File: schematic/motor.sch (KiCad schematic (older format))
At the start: 23 parts, among them U2 TMC2130

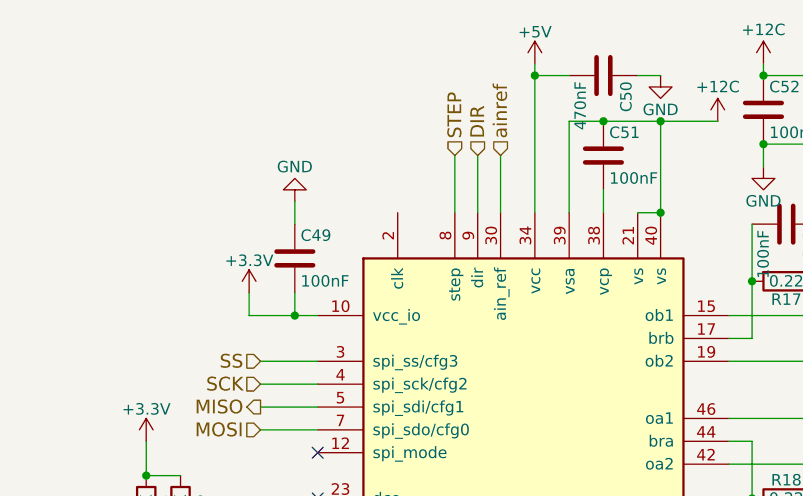
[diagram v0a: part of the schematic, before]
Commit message: Removed some components
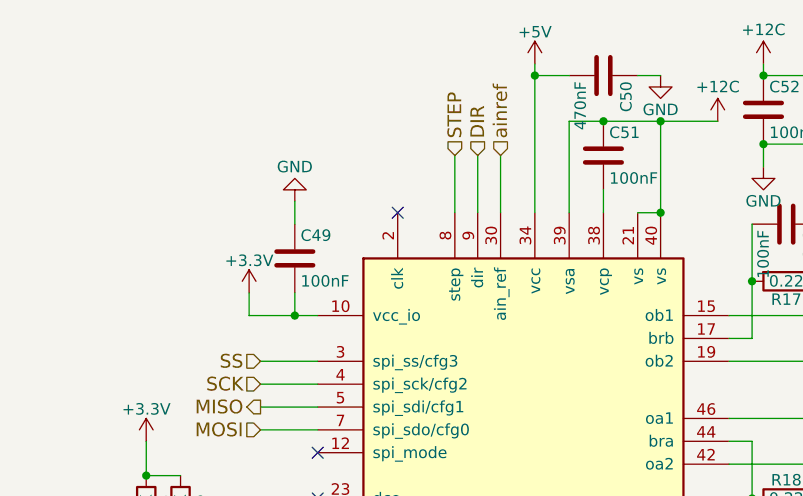
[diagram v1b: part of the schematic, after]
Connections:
- no-connect marks 3 -> 4
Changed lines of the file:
@@
 $Descr A4 11693 8268
 encoding utf-8
-Sheet 1 10
+Sheet 4 10
 Title ""
 Date ""
@@
 DIAG1
 $Comp
-L GND #PWR14
+L GND #PWR27
 U 1 1 59E7A6C8
 P 4050 3700
-AR Path="/59E79F4A/59E7A6C8" Ref="#PWR14"  Part="1"
-AR Path="/59E85192/59E7A6C8" Ref="#PWR29"  Part="1"
-AR Path="/59E85CD9/59E7A6C8" Ref="#PWR44"  Part="1"
-AR Path="/59E88785/59E7A6C8" Ref="#PWR59"  Part="1"
-F 0 "#PWR59" H 4050 3450 50  0001 C CNN
+AR Path="/59E79F4A/59E7A6C8" Ref="#PWR27"  Part="1"
+AR Path="/59E85192/59E7A6C8" Ref="#PWR42"  Part="1"
+AR Path="/59E85CD9/59E7A6C8" Ref="#PWR57"  Part="1"
+AR Path="/59E88785/59E7A6C8" Ref="#PWR72"  Part="1"
+F 0 "#PWR72" H 4050 3450 50  0001 C CNN
 F 1 "GND" H 4050 3550 50  0000 C CNN
 F 2 "" H 4050 3700 50  0001 C CNN
@@
 $EndComp
 $Comp
-L +3.3V #PWR12
+L +3.3V #PWR25
 U 1 1 59E7ABA2
 P 3550 3350
-AR Path="/59E79F4A/59E7ABA2" Ref="#PWR12"  Part="1"
-AR Path="/59E85192/59E7ABA2" Ref="#PWR27"  Part="1"
-AR Path="/59E85CD9/59E7ABA2" Ref="#PWR42"  Part="1"
-AR Path="/59E88785/59E7ABA2" Ref="#PWR57"  Part="1"
-F 0 "#PWR57" H 3550 3200 50  0001 C CNN
+AR Path="/59E79F4A/59E7ABA2" Ref="#PWR25"  Part="1"
+AR Path="/59E85192/59E7ABA2" Ref="#PWR40"  Part="1"
+AR Path="/59E85CD9/59E7ABA2" Ref="#PWR55"  Part="1"
+AR Path="/59E88785/59E7ABA2" Ref="#PWR70"  Part="1"
+F 0 "#PWR70" H 3550 3200 50  0001 C CNN
 F 1 "+3.3V" H 3550 3490 50  0000 C CNN
 F 2 "" H 3550 3350 50  0001 C CNN
@@
 DIR
 $Comp
-L GND #PWR16
+L GND #PWR29
 U 1 1 59E7AD62
 P 4200 4800
-AR Path="/59E79F4A/59E7AD62" Ref="#PWR16"  Part="1"
-AR Path="/59E85192/59E7AD62" Ref="#PWR31"  Part="1"
-AR Path="/59E85CD9/59E7AD62" Ref="#PWR46"  Part="1"
-AR Path="/59E88785/59E7AD62" Ref="#PWR61"  Part="1"
-F 0 "#PWR61" H 4200 4550 50  0001 C CNN
+AR Path="/59E79F4A/59E7AD62" Ref="#PWR29"  Part="1"
+AR Path="/59E85192/59E7AD62" Ref="#PWR44"  Part="1"
+AR Path="/59E85CD9/59E7AD62" Ref="#PWR59"  Part="1"
+AR Path="/59E88785/59E7AD62" Ref="#PWR74"  Part="1"
+F 0 "#PWR74" H 4200 4550 50  0001 C CNN
 F 1 "GND" H 4200 4650 50  0000 C CNN
 F 2 "" H 4200 4800 50  0001 C CNN
@@
 $EndComp
 $Comp
-L GND #PWR17
+L GND #PWR30
 U 1 1 59E7AE9D
 P 4600 5300
-AR Path="/59E79F4A/59E7AE9D" Ref="#PWR17"  Part="1"
-AR Path="/59E85192/59E7AE9D" Ref="#PWR32"  Part="1"
-AR Path="/59E85CD9/59E7AE9D" Ref="#PWR47"  Part="1"
-AR Path="/59E88785/59E7AE9D" Ref="#PWR62"  Part="1"
-F 0 "#PWR62" H 4600 5050 50  0001 C CNN
+AR Path="/59E79F4A/59E7AE9D" Ref="#PWR30"  Part="1"
+AR Path="/59E85192/59E7AE9D" Ref="#PWR45"  Part="1"
+AR Path="/59E85CD9/59E7AE9D" Ref="#PWR60"  Part="1"
+AR Path="/59E88785/59E7AE9D" Ref="#PWR75"  Part="1"
+F 0 "#PWR75" H 4600 5050 50  0001 C CNN
 F 1 "GND" H 4600 5150 50  0000 C CNN
 F 2 "" H 4600 5300 50  0001 C CNN
@@
 $EndComp
 $Comp
-L +5V #PWR18
+L +5V #PWR16
 U 1 1 59E7B341
 P 5250 1700
-AR Path="/59E79F4A/59E7B341" Ref="#PWR18"  Part="1"
-AR Path="/59E85192/59E7B341" Ref="#PWR33"  Part="1"
-AR Path="/59E85CD9/59E7B341" Ref="#PWR48"  Part="1"
-AR Path="/59E88785/59E7B341" Ref="#PWR63"  Part="1"
-F 0 "#PWR63" H 5250 1550 50  0001 C CNN
+AR Path="/59E79F4A/59E7B341" Ref="#PWR16"  Part="1"
+AR Path="/59E85192/59E7B341" Ref="#PWR31"  Part="1"
+AR Path="/59E85CD9/59E7B341" Ref="#PWR46"  Part="1"
+AR Path="/59E88785/59E7B341" Ref="#PWR61"  Part="1"
+F 0 "#PWR61" H 5250 1550 50  0001 C CNN
 F 1 "+5V" H 5250 1840 50  0000 C CNN
 F 2 "" H 5250 1700 50  0001 C CNN
@@
 $EndComp
 $Comp
-L +3.3V #PWR13
+L +3.3V #PWR23
 U 1 1 59E7B49B
 P 4000 2700
-AR Path="/59E79F4A/59E7B49B" Ref="#PWR13"  Part="1"
-AR Path="/59E85192/59E7B49B" Ref="#PWR28"  Part="1"
-AR Path="/59E85CD9/59E7B49B" Ref="#PWR43"  Part="1"
-AR Path="/59E88785/59E7B49B" Ref="#PWR58"  Part="1"
-F 0 "#PWR58" H 4000 2550 50  0001 C CNN
+AR Path="/59E79F4A/59E7B49B" Ref="#PWR23"  Part="1"
+AR Path="/59E85192/59E7B49B" Ref="#PWR38"  Part="1"
+AR Path="/59E85CD9/59E7B49B" Ref="#PWR53"  Part="1"
+AR Path="/59E88785/59E7B49B" Ref="#PWR68"  Part="1"
+F 0 "#PWR68" H 4000 2550 50  0001 C CNN
 F 1 "+3.3V" H 4000 2840 50  0000 C CNN
 F 2 "" H 4000 2700 50  0001 C CNN
@@
 $EndComp
 $Comp
-L GND #PWR15
+L GND #PWR21
 U 1 1 59E7B4C1
 P 4200 2300
-AR Path="/59E79F4A/59E7B4C1" Ref="#PWR15"  Part="1"
-AR Path="/59E85192/59E7B4C1" Ref="#PWR30"  Part="1"
-AR Path="/59E85CD9/59E7B4C1" Ref="#PWR45"  Part="1"
-AR Path="/59E88785/59E7B4C1" Ref="#PWR60"  Part="1"
-F 0 "#PWR60" H 4200 2050 50  0001 C CNN
+AR Path="/59E79F4A/59E7B4C1" Ref="#PWR21"  Part="1"
+AR Path="/59E85192/59E7B4C1" Ref="#PWR36"  Part="1"
+AR Path="/59E85CD9/59E7B4C1" Ref="#PWR51"  Part="1"
+AR Path="/59E88785/59E7B4C1" Ref="#PWR66"  Part="1"
+F 0 "#PWR66" H 4200 2050 50  0001 C CNN
 F 1 "GND" H 4200 2150 50  0000 C CNN
 F 2 "" H 4200 2300 50  0001 C CNN
@@
 $EndComp
 $Comp
-L GND #PWR19
+L GND #PWR18
 U 1 1 59E7B858
 P 5800 1750
-AR Path="/59E79F4A/59E7B858" Ref="#PWR19"  Part="1"
-AR Path="/59E85192/59E7B858" Ref="#PWR34"  Part="1"
-AR Path="/59E85CD9/59E7B858" Ref="#PWR49"  Part="1"
-AR Path="/59E88785/59E7B858" Ref="#PWR64"  Part="1"
-F 0 "#PWR64" H 5800 1500 50  0001 C CNN
+AR Path="/59E79F4A/59E7B858" Ref="#PWR18"  Part="1"
+AR Path="/59E85192/59E7B858" Ref="#PWR33"  Part="1"
+AR Path="/59E85CD9/59E7B858" Ref="#PWR48"  Part="1"
+AR Path="/59E88785/59E7B858" Ref="#PWR63"  Part="1"
+F 0 "#PWR63" H 5800 1500 50  0001 C CNN
 F 1 "GND" H 5800 1600 50  0000 C CNN
 F 2 "" H 5800 1750 50  0001 C CNN
@@
 $EndComp
 $Comp
-L GND #PWR25
+L GND #PWR24
 U 1 1 59E7C836
 P 7850 2900
-AR Path="/59E79F4A/59E7C836" Ref="#PWR25"  Part="1"
-AR Path="/59E85192/59E7C836" Ref="#PWR40"  Part="1"
-AR Path="/59E85CD9/59E7C836" Ref="#PWR55"  Part="1"
-AR Path="/59E88785/59E7C836" Ref="#PWR70"  Part="1"
-F 0 "#PWR70" H 7850 2650 50  0001 C CNN
+AR Path="/59E79F4A/59E7C836" Ref="#PWR24"  Part="1"
+AR Path="/59E85192/59E7C836" Ref="#PWR39"  Part="1"
+AR Path="/59E85CD9/59E7C836" Ref="#PWR54"  Part="1"
+AR Path="/59E88785/59E7C836" Ref="#PWR69"  Part="1"
+F 0 "#PWR69" H 7850 2650 50  0001 C CNN
 F 1 "GND" H 7850 2750 50  0000 C CNN
 F 2 "" H 7850 2900 50  0001 C CNN
@@
 $EndComp
 $Comp
-L GND #PWR23
+L GND #PWR22
 U 1 1 59E7CE35
 P 6650 2550
-AR Path="/59E79F4A/59E7CE35" Ref="#PWR23"  Part="1"
-AR Path="/59E85192/59E7CE35" Ref="#PWR38"  Part="1"
-AR Path="/59E85CD9/59E7CE35" Ref="#PWR53"  Part="1"
-AR Path="/59E88785/59E7CE35" Ref="#PWR68"  Part="1"
-F 0 "#PWR68" H 6650 2300 50  0001 C CNN
+AR Path="/59E79F4A/59E7CE35" Ref="#PWR22"  Part="1"
+AR Path="/59E85192/59E7CE35" Ref="#PWR37"  Part="1"
+AR Path="/59E85CD9/59E7CE35" Ref="#PWR52"  Part="1"
+AR Path="/59E88785/59E7CE35" Ref="#PWR67"  Part="1"
+F 0 "#PWR67" H 6650 2300 50  0001 C CNN
 F 1 "GND" H 6650 2400 50  0000 C CNN
 F 2 "" H 6650 2550 50  0001 C CNN
@@
 $EndComp
 $Comp
-L GND #PWR24
+L GND #PWR28
 U 1 1 59E7D5D6
 P 6650 3700
-AR Path="/59E79F4A/59E7D5D6" Ref="#PWR24"  Part="1"
-AR Path="/59E85192/59E7D5D6" Ref="#PWR39"  Part="1"
-AR Path="/59E85CD9/59E7D5D6" Ref="#PWR54"  Part="1"
-AR Path="/59E88785/59E7D5D6" Ref="#PWR69"  Part="1"
-F 0 "#PWR69" H 6650 3450 50  0001 C CNN
+AR Path="/59E79F4A/59E7D5D6" Ref="#PWR28"  Part="1"
+AR Path="/59E85192/59E7D5D6" Ref="#PWR43"  Part="1"
+AR Path="/59E85CD9/59E7D5D6" Ref="#PWR58"  Part="1"
+AR Path="/59E88785/59E7D5D6" Ref="#PWR73"  Part="1"
+F 0 "#PWR73" H 6650 3450 50  0001 C CNN
 F 1 "GND" H 6650 3550 50  0000 C CNN
 F 2 "" H 6650 3700 50  0001 C CNN
@@
 Connection ~ 4950 5150
 $Comp
-L +12C #PWR66
+L +12C #PWR62
 U 1 1 5A02A4C9
 P 6250 1700
-AR Path="/59E88785/5A02A4C9" Ref="#PWR66"  Part="1"
-AR Path="/59E79F4A/5A02A4C9" Ref="#PWR21"  Part="1"
-AR Path="/59E85192/5A02A4C9" Ref="#PWR36"  Part="1"
-AR Path="/59E85CD9/5A02A4C9" Ref="#PWR51"  Part="1"
-F 0 "#PWR66" H 6250 1550 50  0001 C CNN
+AR Path="/59E88785/5A02A4C9" Ref="#PWR62"  Part="1"
+AR Path="/59E79F4A/5A02A4C9" Ref="#PWR17"  Part="1"
+AR Path="/59E85192/5A02A4C9" Ref="#PWR32"  Part="1"
+AR Path="/59E85CD9/5A02A4C9" Ref="#PWR47"  Part="1"
+F 0 "#PWR62" H 6250 1550 50  0001 C CNN
 F 1 "+12C" H 6250 1850 50  0000 C CNN
 F 2 "" H 6250 1700 50  0001 C CNN
@@
 $EndComp
 $Comp
-L +12C #PWR65
+L +12C #PWR64
 U 1 1 5A02A509
 P 6050 1950
-AR Path="/59E88785/5A02A509" Ref="#PWR65"  Part="1"
-AR Path="/59E79F4A/5A02A509" Ref="#PWR20"  Part="1"
-AR Path="/59E85192/5A02A509" Ref="#PWR35"  Part="1"
-AR Path="/59E85CD9/5A02A509" Ref="#PWR50"  Part="1"
-F 0 "#PWR65" H 6050 1800 50  0001 C CNN
+AR Path="/59E88785/5A02A509" Ref="#PWR64"  Part="1"
+AR Path="/59E79F4A/5A02A509" Ref="#PWR19"  Part="1"
+AR Path="/59E85192/5A02A509" Ref="#PWR34"  Part="1"
+AR Path="/59E85CD9/5A02A509" Ref="#PWR49"  Part="1"
+F 0 "#PWR64" H 6050 1800 50  0001 C CNN
 F 1 "+12C" H 6050 2100 50  0000 C CNN
 F 2 "" H 6050 1950 50  0001 C CNN
@@
 $EndComp
 $Comp
-L GND #PWR22
+L GND #PWR20
 U 1 1 5A02AD70
 P 6250 2150
-AR Path="/59E79F4A/5A02AD70" Ref="#PWR22"  Part="1"
-AR Path="/59E85192/5A02AD70" Ref="#PWR37"  Part="1"
-AR Path="/59E85CD9/5A02AD70" Ref="#PWR52"  Part="1"
-AR Path="/59E88785/5A02AD70" Ref="#PWR67"  Part="1"
-F 0 "#PWR67" H 6250 1900 50  0001 C CNN
+AR Path="/59E79F4A/5A02AD70" Ref="#PWR20"  Part="1"
+AR Path="/59E85192/5A02AD70" Ref="#PWR35"  Part="1"
+AR Path="/59E85CD9/5A02AD70" Ref="#PWR50"  Part="1"
+AR Path="/59E88785/5A02AD70" Ref="#PWR65"  Part="1"
+F 0 "#PWR65" H 6250 1900 50  0001 C CNN
 F 1 "GND" H 6250 2000 50  0000 C CNN
 F 2 "" H 6250 2150 50  0001 C CNN
@@
 	1    0    0    -1
 $EndComp
+NoConn ~ 4650 2350
 $EndSCHEMATC

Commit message: Updated to kicad v5
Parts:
- C10, C11, C12, C13, C14, C16, C17, C18, C19, C6, C7, C8, C9: symbol C -> schematic-rescue:C
- C15: symbol CP -> schematic-rescue:CP
- L1, L2, L3, L4: symbol Ferrite_Bead_Small -> schematic-rescue:Ferrite_Bead_Small
- R3, R4, R5, R6: symbol R -> schematic-rescue:R
- U2: symbol TMC2130 -> tmc2130:TMC2130
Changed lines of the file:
@@
-EESchema Schematic File Version 2
-LIBS:bd9e302efj
-LIBS:psmn1
-LIBS:tmc2130
-LIBS:74xgxx
-LIBS:74xx
-LIBS:ac-dc
-LIBS:actel
-LIBS:adc-dac
-LIBS:allegro
-LIBS:Altera
-LIBS:analog_devices
-LIBS:analog_switches
-LIBS:atmel
-LIBS:audio
-LIBS:battery_management
-LIBS:bbd
-LIBS:bosch
-LIBS:brooktre
-LIBS:cmos4000
-LIBS:cmos_ieee
-LIBS:conn
-LIBS:contrib
-LIBS:cypress
-LIBS:dc-dc
-LIBS:device
-LIBS:digital-audio
-LIBS:diode
-LIBS:display
-LIBS:dsp
-LIBS:elec-unifil
-LIBS:ESD_Protection
-LIBS:ftdi
-LIBS:gennum
-LIBS:graphic_symbols
-LIBS:hc11
-LIBS:infineon
-LIBS:intel
-LIBS:interface
-LIBS:intersil
-LIBS:ir
-LIBS:Lattice
-LIBS:leds
-LIBS:LEM
-LIBS:linear
-LIBS:logic_programmable
-LIBS:maxim
-LIBS:mechanical
-LIBS:memory
-LIBS:microchip
-LIBS:microchip_dspic33dsc
-LIBS:microchip_pic10mcu
-LIBS:microchip_pic12mcu
-LIBS:microchip_pic16mcu
-LIBS:microchip_pic18mcu
-LIBS:microchip_pic24mcu
-LIBS:microchip_pic32mcu
-LIBS:microcontrollers
-LIBS:modules
-LIBS:motor_drivers
-LIBS:motorola
-LIBS:motors
-LIBS:msp430
-LIBS:nordicsemi
-LIBS:nxp
-LIBS:nxp_armmcu
-LIBS:onsemi
-LIBS:opto
-LIBS:Oscillators
-LIBS:philips
-LIBS:power
-LIBS:powerint
-LIBS:Power_Management
-LIBS:pspice
-LIBS:references
-LIBS:regul
-LIBS:relays
-LIBS:rfcom
-LIBS:RFSolutions
-LIBS:sensors
-LIBS:silabs
-LIBS:siliconi
-LIBS:stm8
-LIBS:stm32
-LIBS:supertex
-LIBS:switches
-LIBS:texas
-LIBS:transf
-LIBS:transistors
-LIBS:triac_thyristor
-LIBS:ttl_ieee
-LIBS:valves
-LIBS:video
-LIBS:wiznet
-LIBS:Worldsemi
-LIBS:Xicor
-LIBS:xilinx
-LIBS:zetex
-LIBS:Zilog
+EESchema Schematic File Version 4
 LIBS:schematic-cache
-EELAYER 25 0
+EELAYER 26 0
 EELAYER END
 $Descr A4 11693 8268
@@
 SCK
 $Comp
-L TMC2130 U2
+L tmc2130:TMC2130 U2
 U 1 1 59E7A3F7
 P 5200 3750
@@
 DIAG1
 $Comp
-L GND #PWR017
+L power:GND #PWR017
 U 1 1 59E7A6C8
 P 4050 3700
@@
 DIAG0
 $Comp
-L R R4
+L schematic-rescue:R R4
 U 1 1 59E7AAF8
 P 3700 3650
@@
 $EndComp
 $Comp
-L R R3
+L schematic-rescue:R R3
 U 1 1 59E7AB4D
 P 3550 3650
@@
 $EndComp
 $Comp
-L +3.3V #PWR018
+L power:+3.3V #PWR018
 U 1 1 59E7ABA2
 P 3550 3350
@@
 DIR
 $Comp
-L GND #PWR019
+L power:GND #PWR019
 U 1 1 59E7AD62
 P 4200 4800
@@
 $EndComp
 $Comp
-L GND #PWR020
+L power:GND #PWR020
 U 1 1 59E7AE9D
 P 4600 5300
@@
 $EndComp
 $Comp
-L C C9
+L schematic-rescue:C C9
 U 1 1 59E7B152
 P 5550 2100
@@
 AR Path="/59E85CD9/59E7B152" Ref="C37"  Part="1"
 AR Path="/59E88785/59E7B152" Ref="C51"  Part="1"
+AR Path="/59E7B152" Ref="C51"  Part="1"
 F 0 "C51" H 5575 2200 50  0000 L CNN
 F 1 "100nF" H 5575 2000 50  0000 L CNN
@@
 $EndComp
 $Comp
-L +5V #PWR021
+L power:+5V #PWR021
 U 1 1 59E7B341
 P 5250 1700
@@
 $EndComp
 $Comp
-L C C7
+L schematic-rescue:C C7
 U 1 1 59E7B40E
 P 4200 2550
@@
 AR Path="/59E85CD9/59E7B40E" Ref="C35"  Part="1"
 AR Path="/59E88785/59E7B40E" Ref="C49"  Part="1"
+AR Path="/59E7B40E" Ref="C49"  Part="1"
 F 0 "C49" H 4225 2650 50  0000 L CNN
 F 1 "100nF" H 4225 2450 50  0000 L CNN
@@
 $EndComp
 $Comp
-L +3.3V #PWR022
+L power:+3.3V #PWR022
 U 1 1 59E7B49B
 P 4000 2700
@@
 $EndComp
 $Comp
-L GND #PWR023
+L power:GND #PWR023
 U 1 1 59E7B4C1
 P 4200 2300
@@
 $EndComp
 $Comp
-L C C6
+L schematic-rescue:C C6
 U 1 1 59E7B5DB
 P 3900 4500
@@
 AR Path="/59E85CD9/59E7B5DB" Ref="C34"  Part="1"
 AR Path="/59E88785/59E7B5DB" Ref="C48"  Part="1"
+AR Path="/59E7B5DB" Ref="C48"  Part="1"
 F 0 "C48" H 3925 4600 50  0000 L CNN
 F 1 "4.7uF" H 3925 4400 50  0000 L CNN
@@
 $EndComp
 $Comp
-L C C8
+L schematic-rescue:C C8
 U 1 1 59E7B7C5
 P 5550 1750
@@
 AR Path="/59E85CD9/59E7B7C5" Ref="C36"  Part="1"
 AR Path="/59E88785/59E7B7C5" Ref="C50"  Part="1"
+AR Path="/59E7B7C5" Ref="C50"  Part="1"
 F 0 "C50" H 5575 1850 50  0000 L CNN
 F 1 "470nF" H 5575 1650 50  0000 L CNN
@@
 $EndComp
 $Comp
-L GND #PWR024
+L power:GND #PWR024
 U 1 1 59E7B858
 P 5800 1750
@@
 $EndComp
 $Comp
-L C C10
+L schematic-rescue:C C10
 U 1 1 59E7BC4E
 P 6250 1900
@@
 AR Path="/59E85CD9/59E7BC4E" Ref="C38"  Part="1"
 AR Path="/59E88785/59E7BC4E" Ref="C52"  Part="1"
+AR Path="/59E7BC4E" Ref="C52"  Part="1"
 F 0 "C52" H 6275 2000 50  0000 L CNN
 F 1 "100nF" H 6275 1800 50  0000 L CNN
@@
 $EndComp
 $Comp
-L C C14
+L schematic-rescue:C C14
 U 1 1 59E7BC86
 P 6550 1900
@@
 AR Path="/59E85CD9/59E7BC86" Ref="C42"  Part="1"
 AR Path="/59E88785/59E7BC86" Ref="C56"  Part="1"
+AR Path="/59E7BC86" Ref="C56"  Part="1"
 F 0 "C56" H 6575 2000 50  0000 L CNN
 F 1 "100nF" H 6575 1800 50  0000 L CNN
@@
 $EndComp
 $Comp
-L CP C15
+L schematic-rescue:CP C15
 U 1 1 59E7BCBF
 P 6850 1900
@@
 $EndComp
 $Comp
-L C C16
+L schematic-rescue:C C16
 U 1 1 59E7BFFD
 P 7650 2800
@@
 AR Path="/59E85CD9/59E7BFFD" Ref="C44"  Part="1"
 AR Path="/59E88785/59E7BFFD" Ref="C58"  Part="1"
+AR Path="/59E7BFFD" Ref="C58"  Part="1"
 F 0 "C58" H 7675 2900 50  0000 L CNN
 F 1 "1nF" H 7675 2700 50  0000 L CNN
@@
 $EndComp
 $Comp
-L C C17
+L schematic-rescue:C C17
 U 1 1 59E7C1A8
 P 7650 3000
@@
 AR Path="/59E85CD9/59E7C1A8" Ref="C45"  Part="1"
 AR Path="/59E88785/59E7C1A8" Ref="C59"  Part="1"
+AR Path="/59E7C1A8" Ref="C59"  Part="1"
 F 0 "C59" H 7675 3100 50  0000 L CNN
 F 1 "1nF" H 7675 2900 50  0000 L CNN
@@
 $EndComp
 $Comp
-L Ferrite_Bead_Small L1
+L schematic-rescue:Ferrite_Bead_Small L1
 U 1 1 59E7C37A
 P 8250 2600
@@
 $EndComp
 $Comp
-L Ferrite_Bead_Small L2
+L schematic-rescue:Ferrite_Bead_Small L2
 U 1 1 59E7C44D
 P 8250 3000
@@
 $EndComp
 $Comp
-L GND #PWR025
+L power:GND #PWR025
 U 1 1 59E7C836
 P 7850 2900
@@
 $EndComp
 $Comp
-L C C11
+L schematic-rescue:C C11
 U 1 1 59E7CC9C
 P 6350 2400
@@
 AR Path="/59E85CD9/59E7CC9C" Ref="C39"  Part="1"
 AR Path="/59E88785/59E7CC9C" Ref="C53"  Part="1"
+AR Path="/59E7CC9C" Ref="C53"  Part="1"
 F 0 "C53" H 6375 2500 50  0000 L CNN
 F 1 "100nF" H 6375 2300 50  0000 L CNN
@@
 $EndComp
 $Comp
-L R R5
+L schematic-rescue:R R5
 U 1 1 59E7CD25
 P 6350 2650
@@
 $EndComp
 $Comp
-L GND #PWR026
+L power:GND #PWR026
 U 1 1 59E7CE35
 P 6650 2550
@@
 Connection ~ 6200 2650
 $Comp
-L C C12
+L schematic-rescue:C C12
 U 1 1 59E7D5CA
 P 6350 3850
@@
 AR Path="/59E85CD9/59E7D5CA" Ref="C40"  Part="1"
 AR Path="/59E88785/59E7D5CA" Ref="C54"  Part="1"
+AR Path="/59E7D5CA" Ref="C54"  Part="1"
 F 0 "C54" H 6375 3950 50  0000 L CNN
 F 1 "100nF" H 6375 3750 50  0000 L CNN
@@
 $EndComp
 $Comp
-L R R6
+L schematic-rescue:R R6
 U 1 1 59E7D5D0
 P 6350 3600
@@
 $EndComp
 $Comp
-L GND #PWR027
+L power:GND #PWR027
 U 1 1 59E7D5D6
 P 6650 3700
@@
 Connection ~ 6200 3600
 $Comp
-L C C13
+L schematic-rescue:C C13
 U 1 1 59E7AFF0
 P 6350 4100
@@
 AR Path="/59E85CD9/59E7AFF0" Ref="C41"  Part="1"
 AR Path="/59E88785/59E7AFF0" Ref="C55"  Part="1"
+AR Path="/59E7AFF0" Ref="C55"  Part="1"
 F 0 "C55" H 6375 4200 50  0000 L CNN
 F 1 "22n" H 6375 4000 50  0000 L CNN
@@
 	6200 3350 6100 3350
 $Comp
-L C C19
+L schematic-rescue:C C19
 U 1 1 59E7DC97
 P 7650 3450
@@
 AR Path="/59E85CD9/59E7DC97" Ref="C47"  Part="1"
 AR Path="/59E88785/59E7DC97" Ref="C61"  Part="1"
+AR Path="/59E7DC97" Ref="C61"  Part="1"
 F 0 "C61" H 7675 3550 50  0000 L CNN
 F 1 "1nF" H 7675 3350 50  0000 L CNN
@@
 $EndComp
 $Comp
-L C C18
+L schematic-rescue:C C18
 U 1 1 59E7DC9D
 P 7650 3250
@@
 AR Path="/59E85CD9/59E7DC9D" Ref="C46"  Part="1"
 AR Path="/59E88785/59E7DC9D" Ref="C60"  Part="1"
+AR Path="/59E7DC9D" Ref="C60"  Part="1"
 F 0 "C60" H 7675 3350 50  0000 L CNN
 F 1 "1nF" H 7675 3150 50  0000 L CNN
@@
 $EndComp
 $Comp
-L Ferrite_Bead_Small L4
+L schematic-rescue:Ferrite_Bead_Small L4
 U 1 1 59E7DCA3
 P 8250 3650
@@
 $EndComp
 $Comp
-L Ferrite_Bead_Small L3
+L schematic-rescue:Ferrite_Bead_Small L3
 U 1 1 59E7DCA9
 P 8250 3250
@@
 $EndComp
 $Comp
-L GND #PWR028
+L power:GND #PWR028
 U 1 1 59E7DCAF
 P 7850 3350
@@
 Connection ~ 4950 5150
 $Comp
-L +12C #PWR074
+L power:+12C #PWR074
 U 1 1 5A02A4C9
 P 6250 1700
@@
 $EndComp
 $Comp
-L +12C #PWR075
+L power:+12C #PWR075
 U 1 1 5A02A509
 P 6050 1950
@@
 $EndComp
 $Comp
-L GND #PWR031
+L power:GND #PWR031
 U 1 1 5A02AD70
 P 6250 2150

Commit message: Moved to L6470 driver
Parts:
- removed C10, C11, C12, C7, C9: 100nF, Capacitors_SMD:C_0603, symbol schematic-rescue:C
- removed C13: 22n, Capacitors_SMD:C_0603, symbol schematic-rescue:C
- removed C16, C17, C18, C19: 1nF, Capacitors_SMD:C_0603, symbol schematic-rescue:C
- removed C6: 4.7uF, Capacitors_SMD:C_0805, symbol schematic-rescue:C
- removed C8: 470nF, Capacitors_SMD:C_0603, symbol schematic-rescue:C
- removed L1, L2, L3, L4: 120R, Inductors_SMD:L_0603, symbol schematic-rescue:Ferrite_Bead_Small
- removed R3, R4: 10K, Resistors_SMD:R_0603, symbol schematic-rescue:R
- removed R5, R6: 0.22, Resistors_SMD:R_1206, symbol schematic-rescue:R
- removed U2: TMC2130, tmc2130:TQFP-48-1EP_7x7mm_Pitch0.5mm, symbol tmc2130:TMC2130
- added C13: 10nF, Capacitor_SMD:C_0603_1608Metric, symbol Device:C
- added C6: 100nF, Capacitor_SMD:C_0603_1608Metric, symbol Device:C
- added C7: 22uF, Capacitor_SMD:C_1206_3216Metric, symbol Device:C
- added C8: 220nF, Capacitor_SMD:C_0603_1608Metric, symbol Device:C
- added D21: BAV99,215, Package_TO_SOT_SMD:SOT-323_SC-70, symbol Device:D_Schottky_x2_Serial_AKC
- added R10, R9: 39K, Resistor_SMD:R_0603_1608Metric, symbol Device:R
- added U5: L6470, L6470:HTSSOP-28-L6470, symbol l6470:L6470
- C14: value 100nF -> 220nF; footprint Capacitors_SMD:C_0603 -> Capacitor_SMD:C_0603_1608Metric; symbol schematic-rescue:C -> Device:C
- C15: footprint Capacitors_SMD:CP_Elec_8x10 -> Capacitor_SMD:CP_Elec_8x10; symbol schematic-rescue:CP -> Device:CP
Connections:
- net labels added: BUSY, FLAG, STBY, STCK
- net labels removed: +5V, DIAG0, DIAG1, DIR, EN, STEP, ainref
- wire segments 72 -> 52
- no-connect marks 4 -> 2
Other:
- moved on the sheet: C42, C43
